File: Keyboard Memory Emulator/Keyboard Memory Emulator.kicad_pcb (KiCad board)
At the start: 2 copper layers, 99.7 x 60.3 mm, 38 parts, among them J1 Conn_01x05, J2 Conn_01x01_Male, J3 Conn_01x02, J4 Conn_01x03, J5 Conn_01x02, J6 Conn_01x04, J7 Conn_01x05, J8 Conn_02x05_Odd_Even, SW1 PTS636 SL43 LFS, U1 UPD4168C, U10 MC74VHC1G04DBVT1G, U11 ATmega32-16AU, U12 74LV245APWJ, U2 MC74VHC1G04DBVT1G, U3 SN74HC244APWR, U4 SN74HC244APWR, U5 SN74HC244APWR, U6 IS62C256AL-45ULI-TR, U7 74LV245APWJ, U8 SN74HC244APWR, U9 SN74HC244APWR, Y1 32.768kHz

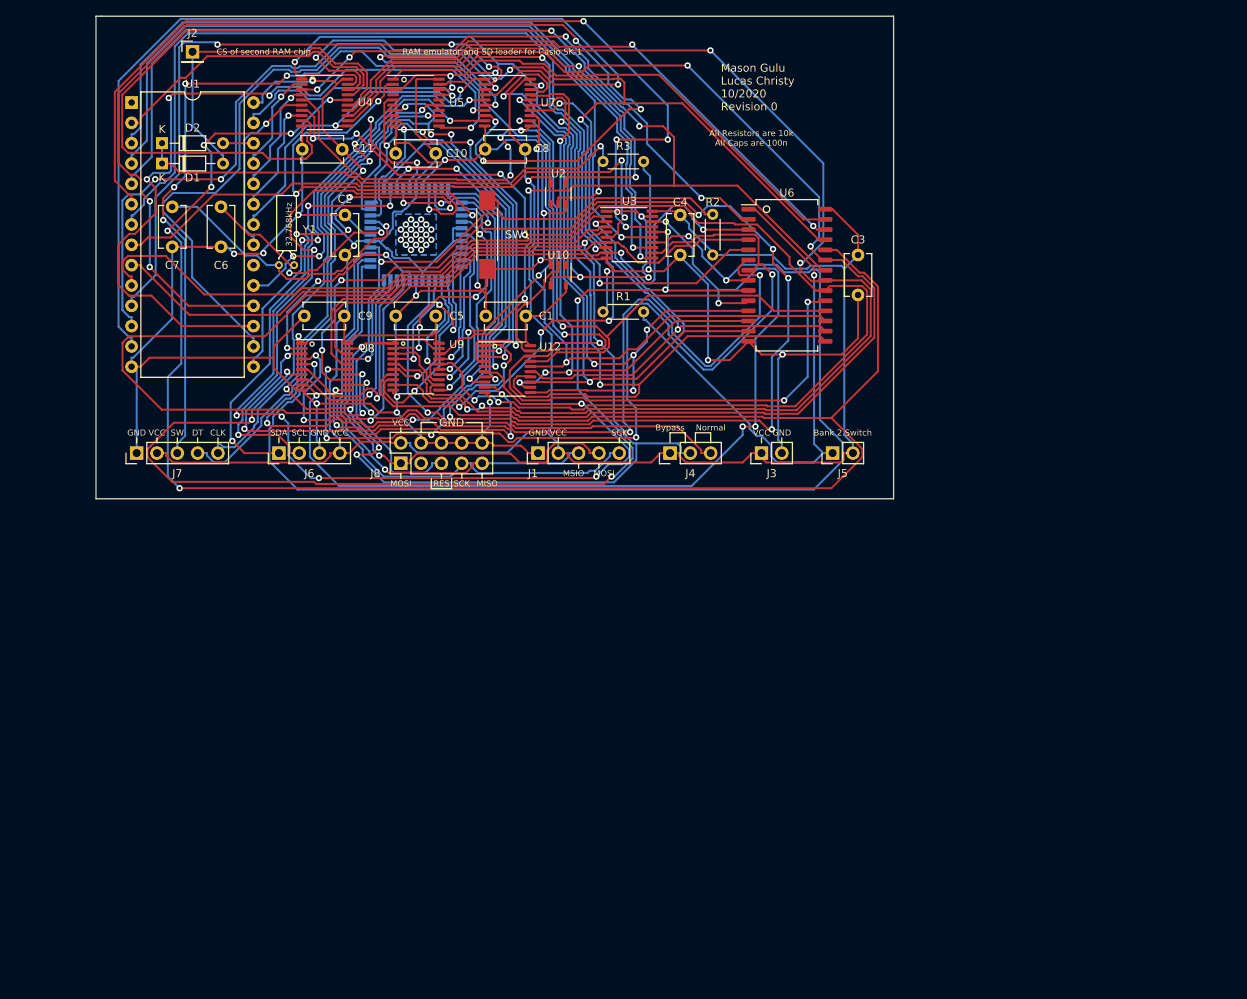
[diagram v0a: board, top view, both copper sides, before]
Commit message: Getting closer to finalization
With this update I believe it should be ready to order, waiting to get it looked over beforehand
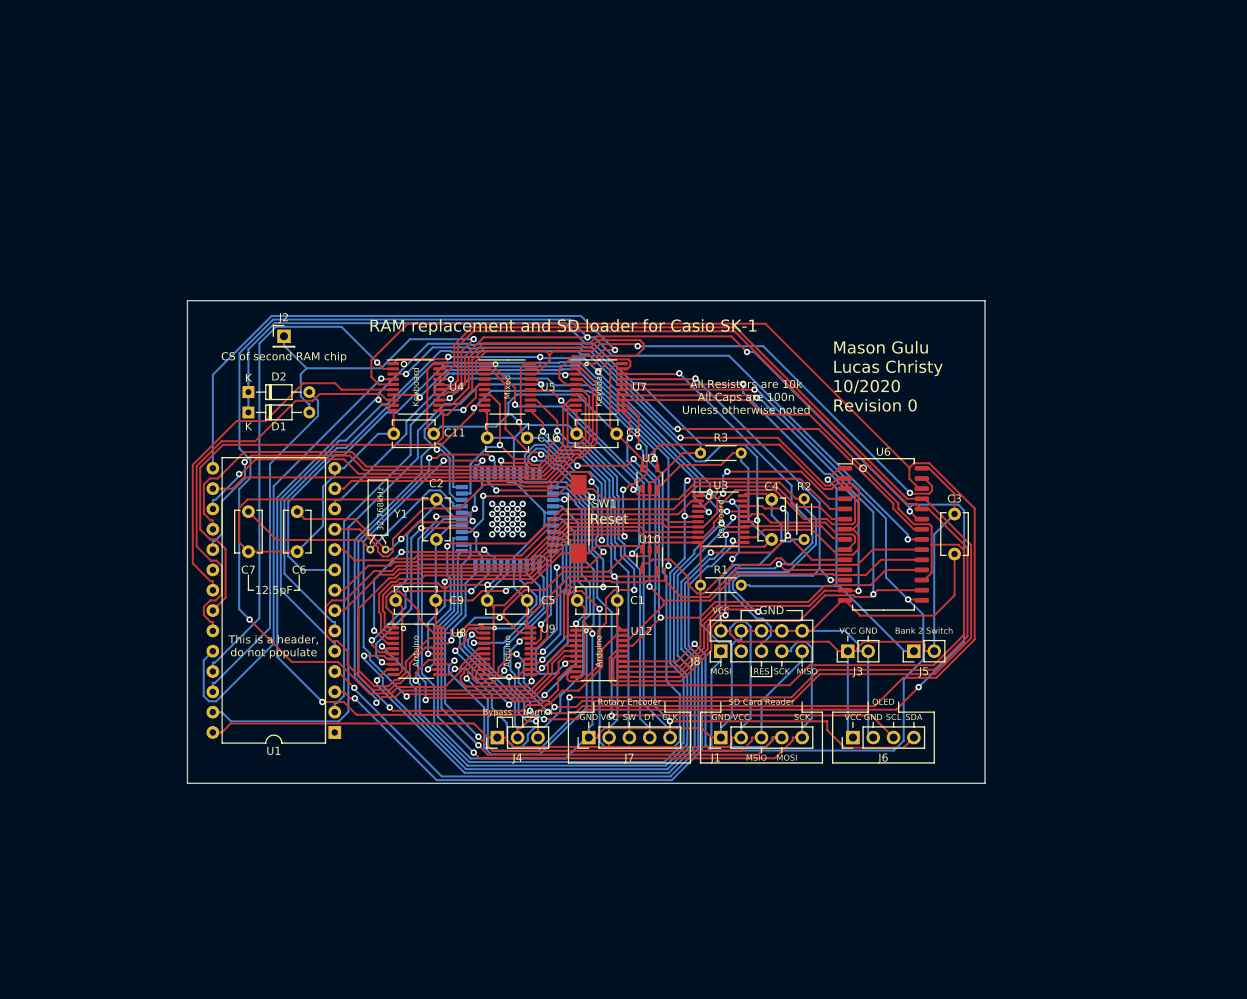
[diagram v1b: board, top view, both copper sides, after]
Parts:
- C6, C7: value 100n -> 12.5p
- moved U1 82.7 mm to (91.4, 125.7), turned to 180 degrees
- moved J6 80.1 mm to (156.2, 126.4)
- moved J7 66.8 mm to (123.2, 126.4)
- moved J8 46.4 mm to (139.7, 115.6)
- moved J1 42.3 mm to (139.7, 126.4)
- moved J4 41.6 mm to (111.8, 126.4)
- moved C6 39.3 mm to (86.7, 103.1)
- moved C7 39.3 mm to (80.6, 103.1)
- moved R3 38.4 mm to (137.2, 90.8)
- moved C1 37.4 mm to (126.7, 109.2)
- moved C10 37.4 mm to (110.5, 88.9)
- moved C5 37.4 mm to (110.5, 109.2)
- moved C9 37.4 mm to (99.1, 109.2)
- moved J2 37.4 mm to (85.1, 76.2)
- moved SW1 37.4 mm to (121.9, 99.1)
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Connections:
- J6 pad 1: SDA -> +5V
- J6 pad 2: SCL -> GND
- J6 pad 3: GND -> SCL
- J6 pad 4: +5V -> SDA
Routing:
- net /AOE: track 151.4 -> 49.1 mm, vias 10 -> 4
- net Net-(U1-Pad18): track 143.3 -> 61.7 mm, vias 6 -> 0
- net Net-(U1-Pad13): track 122.4 -> 44.1 mm, vias 1 -> 0
- net /GA9: track 250.3 -> 174.7 mm, vias 6 -> 2
- net ArduinoEnable: track 194.1 -> 126.1 mm, vias 8 -> 4
- net /PD0: track 52.5 -> 118.9 mm, vias 2 -> 3
- net Net-(U11-Pad13): track 122.2 -> 56.1 mm, vias 7 -> 3
- net GND: track 341.1 -> 400.8 mm, vias 16 -> 2
- net OE: track 42.8 -> 96.9 mm, vias 2 -> 0
- net A3: track 102.2 -> 50.0 mm, vias 1 -> 0
- net Net-(J7-Pad3): track 98.5 -> 47.4 mm, vias 5 -> 1
- net A8: track 13.2 -> 63.3 mm
- net /GA2: track 144.0 -> 96.5 mm, vias 3 -> 2
- net Net-(U11-Pad16): track 101.0 -> 54.3 mm, vias 7 -> 3
- net /GD5: track 73.6 -> 119.9 mm, vias 2 -> 0
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- removed copper zone on B.Cu, net GND
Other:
- board text added: "12.5pF"
- board text added: "All Resistors are 10k All Caps are 100n Unless otherwise noted"
- board text added: "Arduino"
- board text added: "Keyboard"
- board text added: "Mixed"
- board text added: "OLED"
- board text added: "Place headers this direction in place of U1"
- board text added: "RAM replacement and SD loader for Casio SK-1"
- board text added: "Reset"
- board text added: "Rotary Encoder"
- board text added: "SD Card Reader"
- board text added: "This is a header, do not populate"
- board text removed: "All Resistors are 10k All Caps are 100n"
- board text removed: "RAM emulator and SD loader for Casio SK-1"

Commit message: Schematic Restructuring to make it cleaner and easier to read. No actual changes as of yet, but planning to add some pull-up resistors on the I2C data bus.
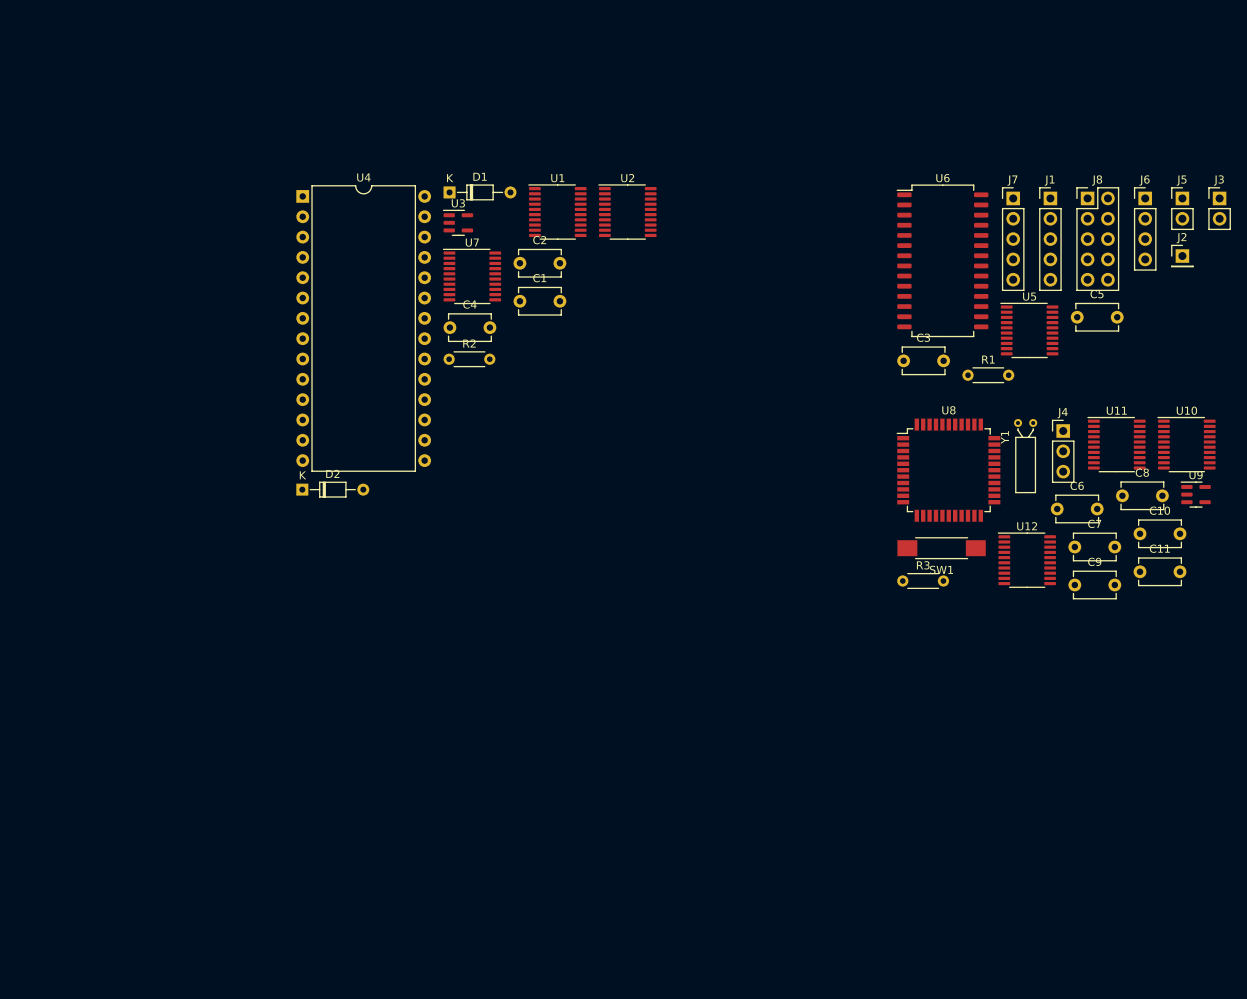
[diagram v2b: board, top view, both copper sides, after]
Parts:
- U1: value UPD4168C -> SN74HC244APWR; footprint Package_DIP:DIP-28_W15.24mm -> Package_SO:TSSOP-20_4.4x6.5mm_P0.65mm
- U10, U2: value MC74VHC1G04DBVT1G -> SN74HC244APWR; footprint Package_SO:thispackagefucker -> Package_SO:TSSOP-20_4.4x6.5mm_P0.65mm
- U11: value ATmega32-16AU -> SN74HC244APWR; footprint Package_QFP:TQFP-44_10x10mm_P0.8mm -> Package_SO:TSSOP-20_4.4x6.5mm_P0.65mm; moved to F.Cu
- U3, U9: value SN74HC244APWR -> MC74VHC1G04DBVT1G; footprint Package_SO:TSSOP-20_4.4x6.5mm_P0.65mm -> inverter:SC-74A
- U4: value SN74HC244APWR -> UPD4168C; footprint Package_SO:TSSOP-20_4.4x6.5mm_P0.65mm -> Package_DIP:DIP-28_W15.24mm
- U8: value SN74HC244APWR -> ATmega32-16AU; footprint Package_SO:TSSOP-20_4.4x6.5mm_P0.65mm -> Package_QFP:TQFP-44_10x10mm_P0.8mm
- moved J2 112.8 mm to (197.4, 66.2)
- moved C7 103.3 mm to (183.9, 102.5), turned to 0 degrees
- moved C6 95.2 mm to (181.7, 97.8), turned to 0 degrees
- moved C11 94.9 mm to (192.1, 105.6)
- moved U9 88.3 mm to (199.1, 96.0)
- moved J7 85.8 mm to (176.2, 59.0), turned to 0 degrees
- moved C9 84.9 mm to (183.9, 107.3)
- moved C10 82.5 mm to (192.1, 100.9)
- moved C5 81.8 mm to (184.2, 73.8)
- moved Y1 80.6 mm to (176.8, 87.0), turned to 0 degrees
- moved J4 80.4 mm to (182.5, 88.0), turned to 0 degrees
- moved J1 79.0 mm to (180.9, 59.0), turned to 0 degrees
- moved U11 76.7 mm to (189.2, 89.7)
- moved J6 76.7 mm to (192.7, 59.0), turned to 0 degrees
- moved J3 73.2 mm to (202.0, 59.0), turned to 0 degrees
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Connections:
- net /GD0 renamed /arduino-side/D0
- net /GD1 renamed /arduino-side/D1
- net /GD2 renamed /arduino-side/D2
- net /GD3 renamed /arduino-side/D3
- net /GD4 renamed /arduino-side/D4
- net /GD5 renamed /arduino-side/D5
- net /GD6 renamed /arduino-side/D6
- net /GD7 renamed /arduino-side/D7
- C1 pad 1: +5V -> GND
- C1 pad 2: GND -> +5V
- C4 pad 1: GND -> +5V
- C4 pad 2: +5V -> GND
- D1 pad 2: CS2 -> CS1
- D2 pad 2: CS1 -> CS2
- R2 pad 1: +5V -> Net-(D1-Pad1)
- R2 pad 2: RESET -> GND
- R3 pad 1: Net-(D1-Pad1) -> +5V
- R3 pad 2: GND -> RESET
- U1 pad 1: Net-(U1-Pad1) -> KeyboardEnable
- U1 pad 10: A0 -> GND
- U1 pad 12: Net-(U1-Pad12) -> /arduino-side/A12
- U1 pad 14: GND -> /arduino-side/CS
- U1 pad 16: Net-(U1-Pad16) -> /arduino-side/A13
- U1 pad 18: Net-(U1-Pad18) -> OE
- U1 pad 19: Net-(U1-Pad19) -> KeyboardEnable
- U1 pad 2: A12 -> OE
- U1 pad 20: Net-(U1-Pad20) -> +5V
- U1 pad 3: A7 -> /arduino-side/A11
- U1 pad 4: A6 -> CS2
- U1 pad 5: A5 -> /arduino-side/A10
- U1 pad 6: A4 -> Net-(U1-Pad6)
- U1 pad 7: A3 -> /arduino-side/A9
- U1 pad 8: A2 -> Net-(U1-Pad8)
- U1 pad 9: A1 -> /arduino-side/A8
- U10 pad 1: (no net) -> ArduinoEnable
- U10 pad 2: ArduinoEnable -> /arduino-side/AOE
- U10 pad 3: GND -> /arduino-side/A11
- U10 pad 4: KeyboardEnable -> Net-(U10-Pad4)
- U10 pad 5: +5V -> /arduino-side/A10
- U11 pad 1: MOSI -> ArduinoEnable
- U11 pad 10: /PD1 -> GND
- U11 pad 11: /PD2 -> PC5
- U11 pad 12: Net-(U11-Pad12) -> /arduino-side/A4
- U11 pad 13: Net-(U11-Pad13) -> PC4
- U11 pad 14: Net-(U11-Pad14) -> /arduino-side/A5
- U11 pad 15: Net-(U11-Pad15) -> PC3
- U11 pad 16: Net-(U11-Pad16) -> /arduino-side/A6
- U11 pad 17: +5V -> Net-(U11-Pad17)
- U11 pad 18: GND -> /arduino-side/A7
- U11 pad 19: SCL -> ArduinoEnable
- U11 pad 2: MISO -> Net-(U11-Pad2)
- U11 pad 20: SDA -> +5V
- U11 pad 3: SCK -> /arduino-side/A3
- U11 pad 4: RESET -> Net-(U11-Pad4)
- U11 pad 5: +5V -> /arduino-side/A2
- U11 pad 6: GND -> Net-(U11-Pad6)
- U11 pad 7: XTAL2 -> /arduino-side/A1
- U11 pad 8: XTAL1 -> Net-(U11-Pad8)
- U11 pad 9: /PD0 -> /arduino-side/A0
- U12 pad 1: /AOE -> /arduino-side/AOE
- U12 pad 2: /PD0 -> /arduino-side/PD0
- U12 pad 3: /PD1 -> /arduino-side/PD1
- U12 pad 4: /PD2 -> /arduino-side/PD2
- U12 pad 5: Net-(U11-Pad12) -> Net-(U12-Pad5)
- U12 pad 6: Net-(U11-Pad13) -> Net-(U12-Pad6)
- U12 pad 7: Net-(U11-Pad14) -> Net-(U12-Pad7)
- U12 pad 8: Net-(U11-Pad15) -> Net-(U12-Pad8)
- U12 pad 9: Net-(U11-Pad16) -> Net-(U12-Pad9)
- U2 pad 1: (no net) -> KeyboardEnable
- U2 pad 2: Net-(D1-Pad1) -> Net-(U2-Pad2)
- U2 pad 3: GND -> /arduino-side/A3
- U2 pad 5: +5V -> /arduino-side/A2
- U3 pad 1: KeyboardEnable -> (no net)
- U3 pad 2: A0 -> Net-(D1-Pad1)
- U3 pad 3: /GA4 -> GND
- U3 pad 4: A1 -> Net-(U1-Pad6)
- U3 pad 5: /GA5 -> +5V
- U4 pad 1: KeyboardEnable -> Net-(U4-Pad1)
- U4 pad 10: GND -> Net-(U2-Pad11)
- U4 pad 11: OE -> Net-(U4-Pad11)
- U4 pad 12: /GA11 -> Net-(U4-Pad12)
- U4 pad 13: Net-(U2-Pad4) -> Net-(U4-Pad13)
- U4 pad 14: /GA10 -> GND
- U4 pad 15: CS2 -> Net-(U4-Pad15)
- U4 pad 16: /GA9 -> Net-(U4-Pad16)
- U4 pad 17: A12 -> Net-(U4-Pad17)
- U4 pad 18: /GA8 -> Net-(U4-Pad18)
- U4 pad 19: KeyboardEnable -> Net-(U4-Pad19)
- U4 pad 2: A8 -> Net-(U1-Pad8)
- U4 pad 20: +5V -> Net-(U4-Pad20)
- U4 pad 3: Net-(U4-Pad3) -> Net-(U2-Pad2)
- U4 pad 4: A9 -> Net-(U2-Pad4)
- U4 pad 5: /GA13 -> Net-(U2-Pad6)
- U4 pad 6: A10 -> Net-(U2-Pad8)
- U4 pad 7: Net-(U4-Pad7) -> Net-(U2-Pad17)
- U4 pad 8: A11 -> Net-(U2-Pad15)
- U4 pad 9: /GOE -> Net-(U2-Pad13)
- U6 pad 10: /GA0 -> /arduino-side/A0
- U6 pad 2: Net-(U4-Pad3) -> /arduino-side/A12
- U6 pad 20: Net-(U4-Pad7) -> /arduino-side/CS
- U6 pad 21: /GA10 -> /arduino-side/A10
- U6 pad 22: /GOE -> OE
- U6 pad 23: /GA11 -> /arduino-side/A11
- U6 pad 24: /GA9 -> /arduino-side/A9
- U6 pad 25: /GA8 -> /arduino-side/A8
- U6 pad 26: /GA13 -> /arduino-side/A13
- U6 pad 27: /GWE -> Net-(U6-Pad27)
- U6 pad 3: /GA7 -> /arduino-side/A7
- U6 pad 4: /GA6 -> /arduino-side/A6
- U6 pad 5: /GA5 -> /arduino-side/A5
- U6 pad 6: /GA4 -> /arduino-side/A4
- U6 pad 7: /GA3 -> /arduino-side/A3
- U6 pad 8: /GA2 -> /arduino-side/A2
- U6 pad 9: /GA1 -> /arduino-side/A1
- U7 pad 2: Net-(U1-Pad11) -> Net-(U4-Pad11)
- U7 pad 3: Net-(U1-Pad12) -> Net-(U4-Pad12)
- U7 pad 4: Net-(U1-Pad13) -> Net-(U4-Pad13)
- U7 pad 5: Net-(U1-Pad15) -> Net-(U4-Pad15)
- U7 pad 6: Net-(U1-Pad16) -> Net-(U4-Pad16)
- U7 pad 7: Net-(U1-Pad17) -> Net-(U4-Pad17)
- U7 pad 8: Net-(U1-Pad18) -> Net-(U4-Pad18)
- U7 pad 9: Net-(U1-Pad19) -> Net-(U4-Pad19)
- U8 pad 1: ArduinoEnable -> MOSI
- U8 pad 10: GND -> /arduino-side/PD1
- U8 pad 11: PC5 -> /arduino-side/PD2
- U8 pad 12: /GA4 -> Net-(U12-Pad5)
- U8 pad 13: PC4 -> Net-(U12-Pad6)
- U8 pad 14: /GA5 -> Net-(U12-Pad7)
- U8 pad 15: PC3 -> Net-(U12-Pad8)
- U8 pad 16: /GA6 -> Net-(U12-Pad9)
- U8 pad 17: Net-(U11-Pad44) -> +5V
- U8 pad 18: /GA7 -> GND
- U8 pad 19: ArduinoEnable -> SCL
- U8 pad 2: Net-(U11-Pad40) -> MISO
- U8 pad 20: +5V -> SDA
- U8 pad 3: /GA3 -> SCK
- U8 pad 4: Net-(U11-Pad41) -> RESET
- U8 pad 5: /GA2 -> +5V
- U8 pad 6: Net-(U11-Pad42) -> GND
- U8 pad 7: /GA1 -> XTAL2
- U8 pad 8: Net-(U11-Pad43) -> XTAL1
- U8 pad 9: /GA0 -> /arduino-side/PD0
- U9 pad 1: ArduinoEnable -> (no net)
- U9 pad 2: /AOE -> ArduinoEnable
- U9 pad 3: /GA11 -> GND
- U9 pad 4: Net-(U11-Pad36) -> KeyboardEnable
- U9 pad 5: /GA10 -> +5V
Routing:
- net GND: track 400.8 -> 0.00 mm, vias 2 -> 0
- net +5V: track 371.9 -> 0.00 mm, vias 3 -> 0
- net /GA10: track 193.2 -> 0.00 mm, vias 3 -> 0
- net /GA13: track 178.8 -> 0.00 mm, vias 2 -> 0
- net /GA11: track 177.4 -> 0.00 mm, vias 6 -> 0
- net /GA9: track 174.7 -> 0.00 mm, vias 2 -> 0
- net /GOE: track 167.6 -> 0.00 mm, vias 5 -> 0
- net /GA8: track 166.6 -> 0.00 mm, vias 2 -> 0
- net ArduinoEnable: track 126.1 -> 0.00 mm, vias 4 -> 0
- net /arduino-side/D3: track 121.0 -> 0.00 mm, vias 3 -> 0
- net /arduino-side/D5: track 119.9 -> 0.00 mm
- net /PD0: track 118.9 -> 0.00 mm, vias 3 -> 0
- net Net-(U4-Pad7): track 115.0 -> 0.00 mm, vias 2 -> 0
- net /GA3: track 107.6 -> 0.00 mm, vias 2 -> 0
- net A5: track 106.1 -> 0.00 mm, vias 1 -> 0
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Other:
- board outline removed
- board text removed: "12.5pF"
- board text removed: "32.768kHz"
- board text removed: "All Resistors are 10k All Caps are 100n Unless otherwise noted"
- board text removed: "Arduino"
- board text removed: "Bank 2 Switch"
- board text removed: "Bypass"
- board text removed: "CLK"
- board text removed: "CS of second RAM chip"
- board text removed: "DT"
- board text removed: "GND"
- board text removed: "Keyboard"
- board text removed: "MISO"
- board text removed: "MOSI"
- board text removed: "MSIO"
- board text removed: "Mason Gulu Lucas Christy 10/2020 Revision 0"
- board text removed: "Mixed"
- board text removed: "Normal"
- board text removed: "OLED"
- board text removed: "Place headers this direction in place of U1"
- board text removed: "RAM replacement and SD loader for Casio SK-1"
- board text removed: "RES"
- board text removed: "Reset"
- board text removed: "Rotary Encoder"
- board text removed: "SCK"
- board text removed: "SCL"
- board text removed: "SD Card Reader"
- board text removed: "SDA"
- board text removed: "SW"
- board text removed: "This is a header, do not populate"
- board text removed: "VCC"

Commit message: Ran the autorouter and updated the PCB
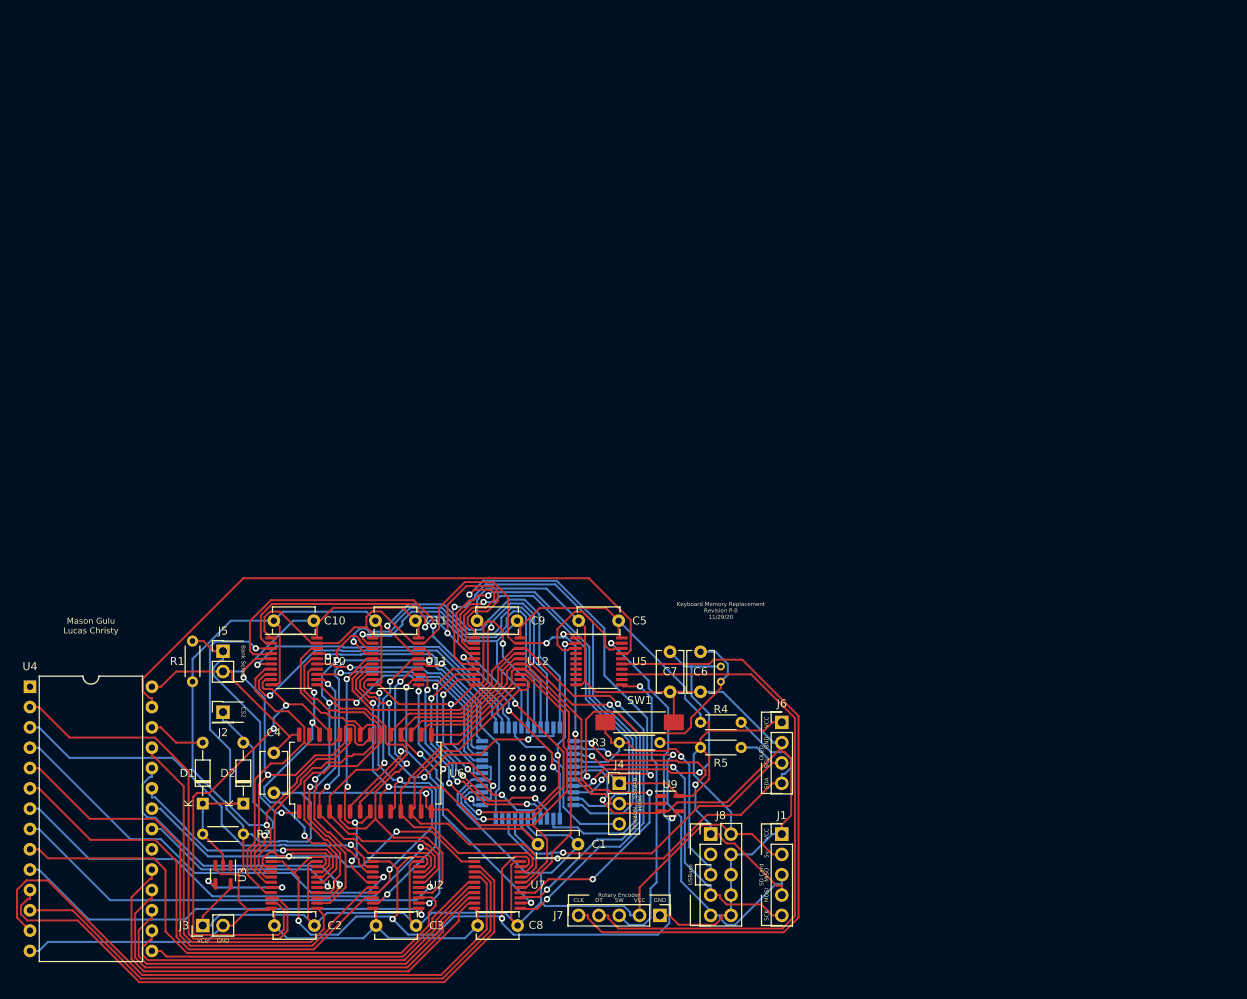
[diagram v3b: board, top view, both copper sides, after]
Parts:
- added R4: 10K, Resistor_THT:R_Axial_DIN0204_L3.6mm_D1.6mm_P5.08mm_Horizontal, F.Cu at (142.2, 124.5)
- added R5: 10K, Resistor_THT:R_Axial_DIN0204_L3.6mm_D1.6mm_P5.08mm_Horizontal, F.Cu at (137.2, 127.6)
- U8, Y1: moved to B.Cu
- moved J3 156.3 mm to (74.9, 149.9), turned to 90 degrees
- moved J2 132.8 mm to (77.5, 123.2)
- moved J5 132.6 mm to (77.5, 115.6)
- moved U10 114.8 mm to (86.4, 116.8)
- moved C10 108.8 mm to (83.8, 111.8)
- moved R1 104.2 mm to (73.7, 119.4), turned to 90 degrees
- moved J7 99.9 mm to (132.1, 148.6), turned to 270 degrees
- moved C8 96.9 mm to (109.3, 149.9)
- moved U6 96.5 mm to (95.2, 130.8), turned to 90 degrees
- moved C11 95.8 mm to (96.5, 111.8)
- moved U11 94.1 mm to (99.1, 116.8)
- moved C3 93.3 mm to (101.6, 149.9), turned to 180 degrees
- moved J8 92.4 mm to (138.4, 138.4)
- moved U1 90.3 mm to (86.4, 144.8)
- moved U2 89.0 mm to (99.1, 144.8)
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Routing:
- net GND: track 0.00 -> 387.9 mm, vias 0 -> 4
- net +5V: track 0.00 -> 340.9 mm
- net KeyboardEnable: track 0.00 -> 138.1 mm, vias 0 -> 5
- net OE: track 0.00 -> 103.5 mm, vias 0 -> 2
- net /arduino-side/AOE: track 0.00 -> 95.9 mm, vias 0 -> 4
- net ArduinoEnable: track 0.00 -> 92.0 mm, vias 0 -> 3
- net Net-(U4-Pad13): track 0.00 -> 79.8 mm
- net Net-(J7-Pad5): track 0.00 -> 79.8 mm
- net Net-(U4-Pad11): track 0.00 -> 78.5 mm
- net KWE: track 0.00 -> 77.6 mm
- net Net-(J7-Pad4): track 0.00 -> 74.7 mm
- net /arduino-side/D7: track 0.00 -> 73.0 mm, vias 0 -> 2
- net Net-(U4-Pad12): track 0.00 -> 72.2 mm
- net Net-(U12-Pad6): track 0.00 -> 69.4 mm, vias 0 -> 1
- net /arduino-side/D4: track 0.00 -> 67.9 mm, vias 0 -> 2
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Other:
- board text added: "5v"
- board text added: "BYPASS"
- board text added: "Bank Select"
- board text added: "CLK"
- board text added: "CS2"
- board text added: "DT"
- board text added: "GND"
- board text added: "Keyboard Memory Replacement Revision P-0 11/29/20"
- board text added: "MISO"
- board text added: "MODE"
- board text added: "MOSI"
- board text added: "Mason Gulu Lucas Christy"
- board text added: "NORMAL"
- board text added: "OLED"
- board text added: "Rotary Encoder"
- board text added: "SCK"
- board text added: "SCL"
- board text added: "SD Card"
- board text added: "SDA"
- board text added: "SW"
- board text added: "USBasp"
- board text added: "VCC"
